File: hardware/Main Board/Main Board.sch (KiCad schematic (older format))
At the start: 17 parts, among them J1 DEC Motor, J2 RA Motor, J3 Battery, J6 Fan, P1 Conn_02x20_Odd_Even, Q6 S8050, U1 ELEGOO, U2 RA Driver, U3 BuckConverter, U4 BuckConverter

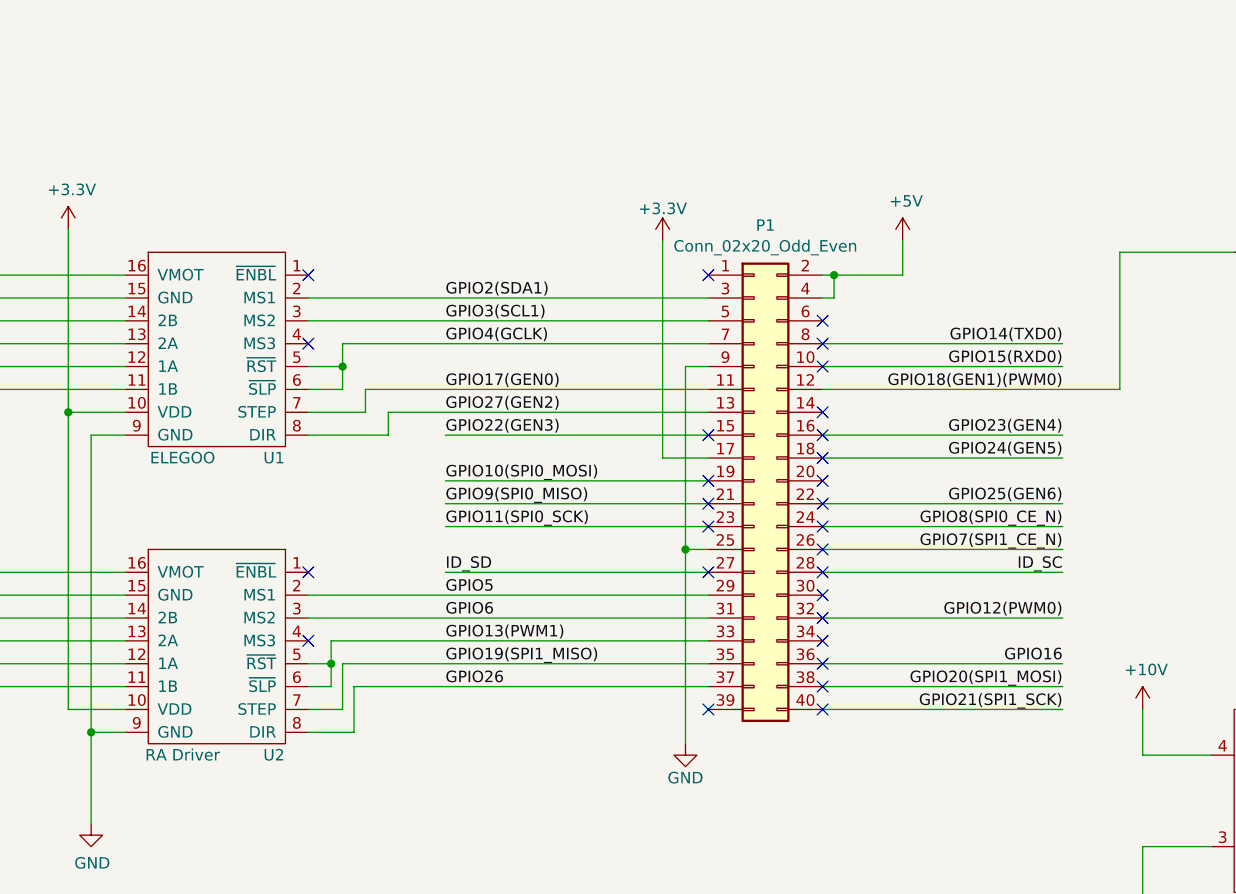
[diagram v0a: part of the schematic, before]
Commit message: Update the Schematic and Route for 2.0
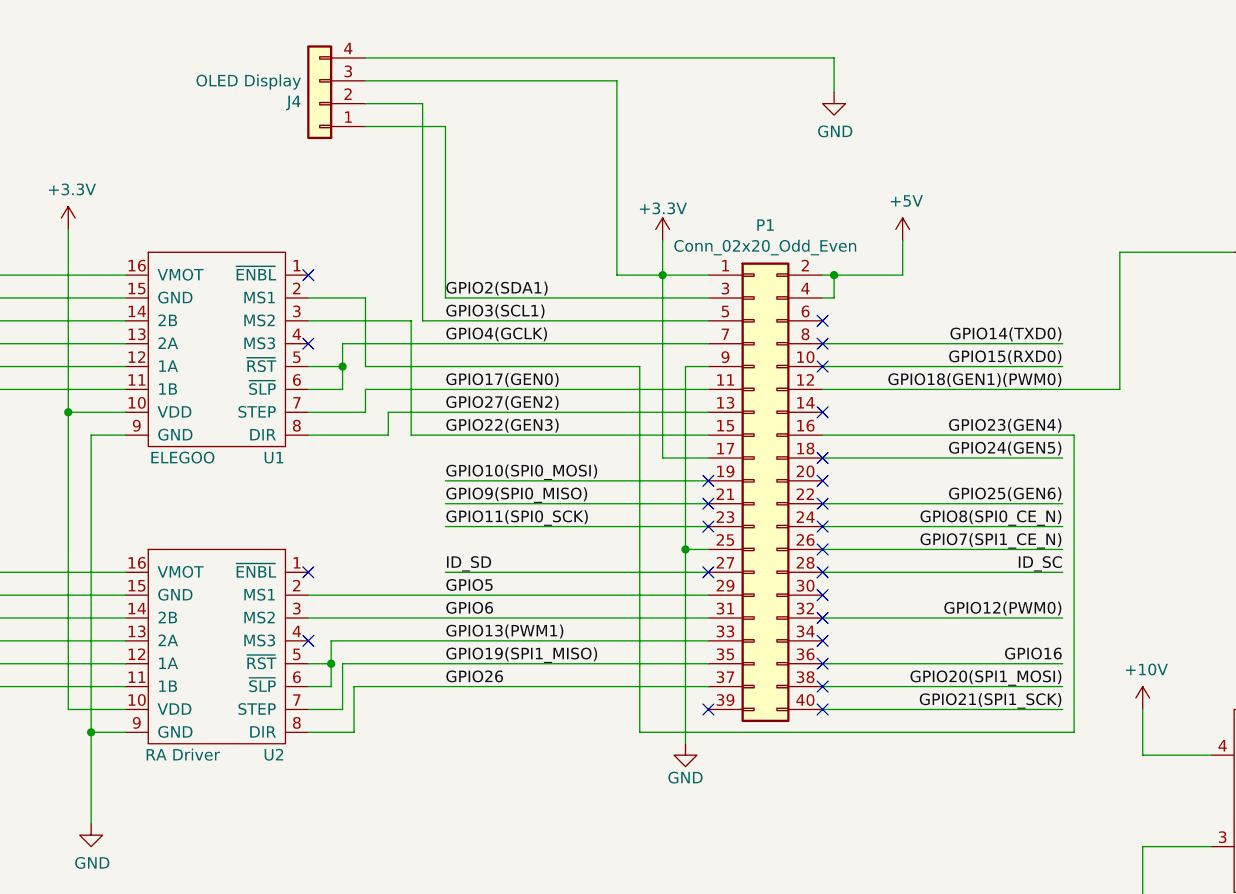
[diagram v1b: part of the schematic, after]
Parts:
- added J4: OLED Display, Connector_JST:JST_PH_B4B-PH-K_1x04_P2.00mm_Vertical, symbol Connector_Generic:Conn_01x04
- J3: footprint Connector_Phoenix_MC_HighVoltage:PhoenixContact_MCV_1,5_2-G-5.08_1x02_P5.08mm_Vertical -> Connector_Wire:SolderWirePad_1x02_P3.81mm_Drill1.2mm
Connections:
- net +3V3: now also P1.1 (Pin_1), J4.3 (Pin_3)
- net GND: now also J4.4 (Pin_4)
- net GPIO2(SDA1): now also J4.1 (Pin_1); no longer U1.2 (MS1)
- net GPIO22(GEN3): now also U1.3 (MS2)
- net GPIO23(GEN4): now also U1.2 (MS1)
- net GPIO3(SCL1): now also J4.2 (Pin_2); no longer U1.3 (MS2)
- no-connect marks 28 -> 25
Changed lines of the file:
@@
 Title "pimount"
 Date "2020-04-22"
-Rev "1.3"
+Rev "2.0"
 Comp ""
 Comment1 "https://github.com/eruditelite/pimount.git"
-Comment2 "release_1.3"
+Comment2 "release_2.0"
 Comment3 ""
 Comment4 ""
@@
 Wire Wire Line
 	7500 3800 8550 3800
-$Comp
-L Connector_Generic:Conn_02x20_Odd_Even P1
-U 1 1 59AD464A
-P 7200 2800
-F 0 "P1" H 7250 3917 50  0000 C CNN
-F 1 "Conn_02x20_Odd_Even" H 7250 3826 50  0000 C CNN
-F 2 "Connector_PinSocket_2.54mm:PinSocket_2x20_P2.54mm_Vertical" H 2350 1850 50  0001 C CNN
-F 3 "" H 2350 1850 50  0001 C CNN
-	1    7200 2800
-	1    0    0    -1
-$EndComp
 Text Label 8550 2200 2    50   ~ 0
 GPIO14(TXD0)
@@
 	7500 2700 8550 2700
 Wire Wire Line
-	7500 2600 8550 2600
-Wire Wire Line
 	7500 3000 8550 3000
 Wire Wire Line
@@
 Wire Wire Line
 	2650 3700 4450 3700
-NoConn ~ 7000 1900
 NoConn ~ 7000 3800
 NoConn ~ 7500 2800
@@
 NoConn ~ 7500 3500
 Wire Wire Line
-	6800 1750 6800 2700
+	6800 1750 6800 1900
 NoConn ~ 7500 2100
 Wire Wire Line
@@
 NoConn ~ 7500 3000
 NoConn ~ 7500 2700
-NoConn ~ 7500 2600
 NoConn ~ 7500 2200
 NoConn ~ 7500 2300
@@
 F 0 "J3" H 10742 5175 50  0000 C CNN
 F 1 "Battery" H 10742 5266 50  0000 C CNN
-F 2 "Connector_Phoenix_MC_HighVoltage:PhoenixContact_MCV_1,5_2-G-5.08_1x02_P5.08mm_Vertical" H 10850 5500 50  0001 C CNN
+F 2 "Connector_Wire:SolderWirePad_1x02_P3.81mm_Drill1.2mm" H 10850 5500 50  0001 C CNN
 F 3 "~" H 10850 5500 50  0001 C CNN
 	1    10850 5500
@@
 Wire Wire Line
 	5400 2200 5400 2300
-Wire Wire Line
-	5250 2100 7000 2100
-Wire Wire Line
-	5250 2000 7000 2000
 Wire Wire Line
 	5250 3300 7000 3300
@@
 	7500 2400 8800 2400
 Wire Wire Line
-	5850 2600 7000 2600
-Wire Wire Line
 	5850 2900 7000 2900
 Wire Wire Line
@@
 NoConn ~ 7000 2900
 NoConn ~ 7000 2800
-NoConn ~ 7000 2600
+$Comp
+L Connector_Generic:Conn_01x04 J4
+U 1 1 5EFB0D93
+P 5300 1150
+F 0 "J4" H 5380 1142 50  0000 L CNN
+F 1 "OLED Display" H 5380 1051 50  0000 L CNN
+F 2 "Connector_JST:JST_PH_B4B-PH-K_1x04_P2.00mm_Vertical" H 5300 1150 50  0001 C CNN
+F 3 "~" H 5300 1150 50  0001 C CNN
+	1    5300 1150
+	-1   0    0    1
+$EndComp
+$Comp
+L Connector_Generic:Conn_02x20_Odd_Even P1
+U 1 1 59AD464A
+P 7200 2800
+F 0 "P1" H 7250 3917 50  0000 C CNN
+F 1 "Conn_02x20_Odd_Even" H 7250 3826 50  0000 C CNN
+F 2 "Connector_PinSocket_2.54mm:PinSocket_2x20_P2.54mm_Vertical" H 2350 1850 50  0001 C CNN
+F 3 "" H 2350 1850 50  0001 C CNN
+	1    7200 2800
+	1    0    0    -1
+$EndComp
+Wire Wire Line
+	8600 2600 8600 3900
+Wire Wire Line
+	8600 3900 6700 3900
+Wire Wire Line
+	6700 3900 6700 2300
+Wire Wire Line
+	6700 2300 5500 2300
+Wire Wire Line
+	7500 2600 8600 2600
+Wire Wire Line
+	7550 950  7550 1100
+$Comp
+L power:GND #PWR03
+U 1 1 5EFE6734
+P 7550 1100
+F 0 "#PWR03" H 7550 850 50  0001 C CNN
+F 1 "GND" H 7555 927 50  0000 C CNN
+F 2 "" H 7550 1100 50  0001 C CNN
+F 3 "" H 7550 1100 50  0001 C CNN
+	1    7550 1100
+	1    0    0    -1
+$EndComp
+Wire Wire Line
+	5500 2000 5250 2000
+Wire Wire Line
+	5500 2000 5500 2300
+Wire Wire Line
+	5850 2000 7000 2000
+Wire Wire Line
+	5700 2600 5700 2100
+Wire Wire Line
+	5700 2100 5250 2100
+Wire Wire Line
+	5700 2600 7000 2600
+Wire Wire Line
+	5750 2100 7000 2100
+Wire Wire Line
+	5500 950  7550 950
+Wire Wire Line
+	5500 1150 5750 1150
+Wire Wire Line
+	5750 1150 5750 2100
+Wire Wire Line
+	5500 1250 5850 1250
+Wire Wire Line
+	5850 1250 5850 2000
+Wire Wire Line
+	7000 1900 6800 1900
+Connection ~ 6800 1900
+Wire Wire Line
+	6800 1900 6800 2700
+Wire Wire Line
+	5500 1050 6600 1050
+Wire Wire Line
+	6600 1050 6600 1900
+Wire Wire Line
+	6600 1900 6800 1900
 $EndSCHEMATC
